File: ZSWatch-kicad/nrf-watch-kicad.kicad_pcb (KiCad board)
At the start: 4 copper layers, 36 x 36 mm, 90 parts, among them IC1 TLV840MAPL36DBVRQ1, IC2 XC9265C181MR-G, IC3 TPS61023DRLT, IC4 MAX30101EFD+T, M1 Vibrator DC Motor, Q1 DMP2045U-7, Q2 SS8050-G, U1 MAX1811ESA+, U2 DMC2400UV-7, U3 LIS2DS12TR, U4 MX25R6435FZNIL0, U5 u-blox ANNA-B402, U6 DRV2603RUNT, U7 XC9265A331MR-G, U8 TXB0104QRUTRQ1, U9 GC9A01

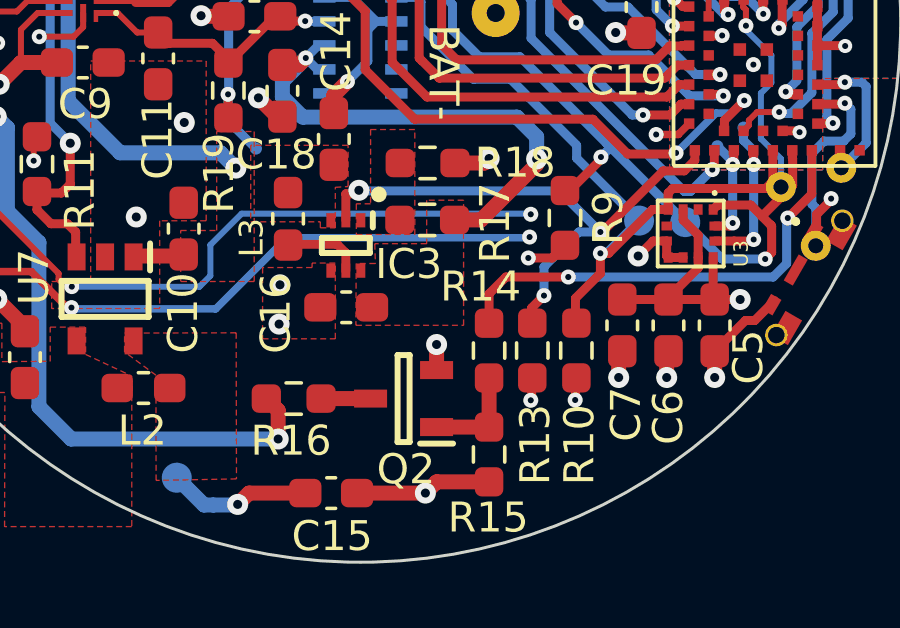
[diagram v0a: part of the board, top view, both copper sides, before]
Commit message: Remove unused parts from v1.
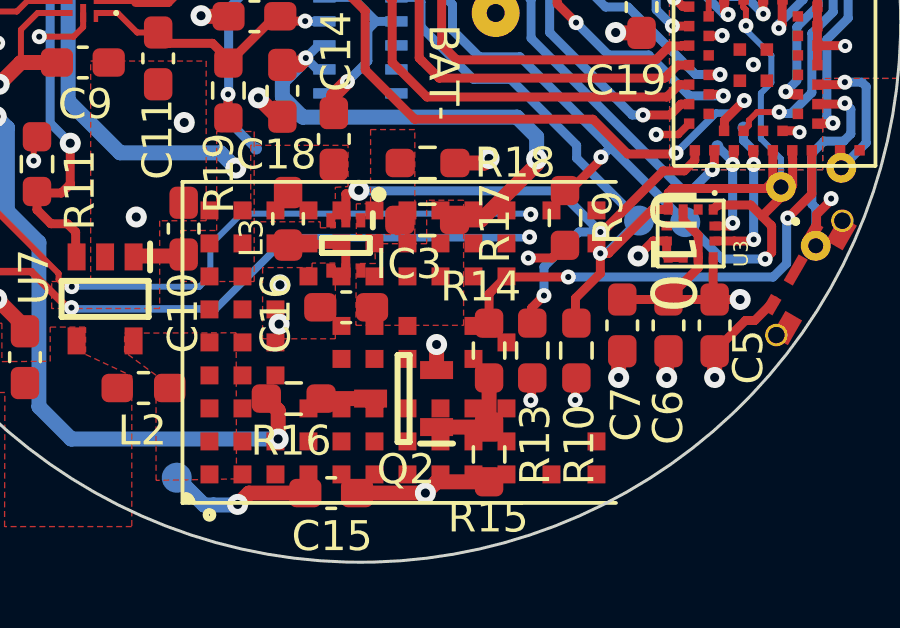
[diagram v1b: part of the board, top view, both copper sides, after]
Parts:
- added U10: 0_NORA-B106, user_library:NORA_LGA82R_1430X1040X180_ANT, F.Cu at (86.4, 106.7)
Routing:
- net SDA_ANNA: track 0.00 -> 56.5 mm, vias 0 -> 4
- net SCL_ANNA: track 56.5 -> 0.00 mm, vias 4 -> 0
- net unconnected-(S2-PadMP1): track 0.00 -> 16.1 mm, vias 0 -> 4
- net BTN_2: track 16.1 -> 0.00 mm, vias 4 -> 0
